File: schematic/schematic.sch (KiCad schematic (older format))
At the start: 19 parts, among them J1 Conn_01x04, J2 Conn_01x04, J3 Conn_01x04, J4 Conn_01x04, J5 Conn_01x04, SW1 SW_Push_Dual, U1 STM32F401VETx, Y1 Crystal_GND24

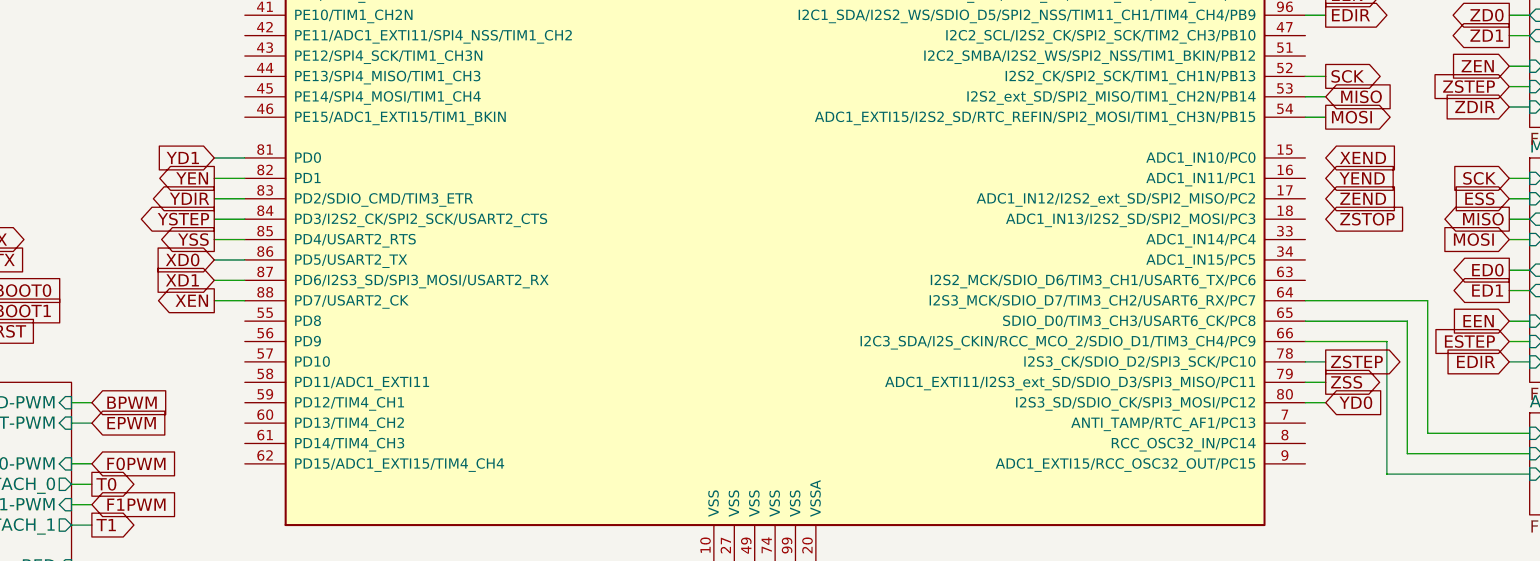
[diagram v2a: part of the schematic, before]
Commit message: Routed all control signals to drivers
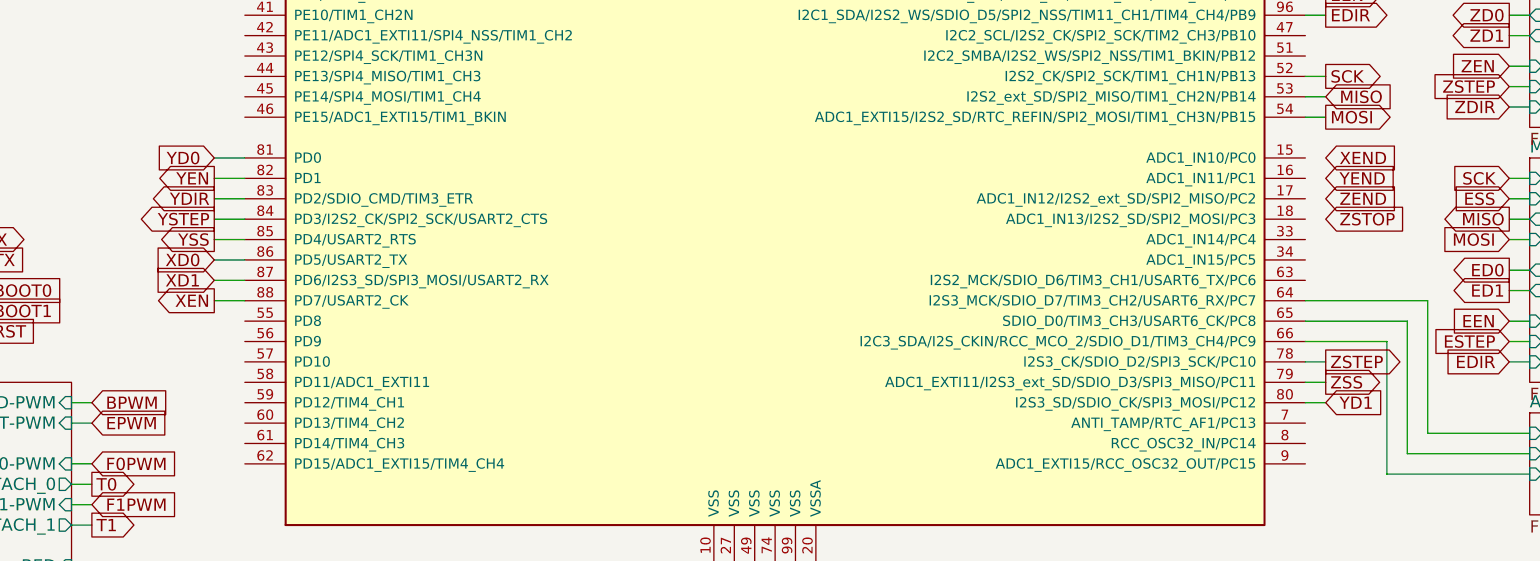
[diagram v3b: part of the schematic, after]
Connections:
- net YD0: now also U1.81 (PD0); no longer U1.80 (I2S3_SD/SDIO_CK/SPI3_MOSI/PC12)
- net YD1: now also U1.80 (I2S3_SD/SDIO_CK/SPI3_MOSI/PC12); no longer U1.81 (PD0)
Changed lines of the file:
@@
 	9100 1250 9200 1250
 Text GLabel 8200 5650 2    60   Input ~ 0
+YD1
+Text GLabel 2750 4450 0    60   Input ~ 0
 YD0
-Text GLabel 2750 4450 0    60   Input ~ 0
-YD1
 Text GLabel 2750 4550 0    60   Output ~ 0
 YEN

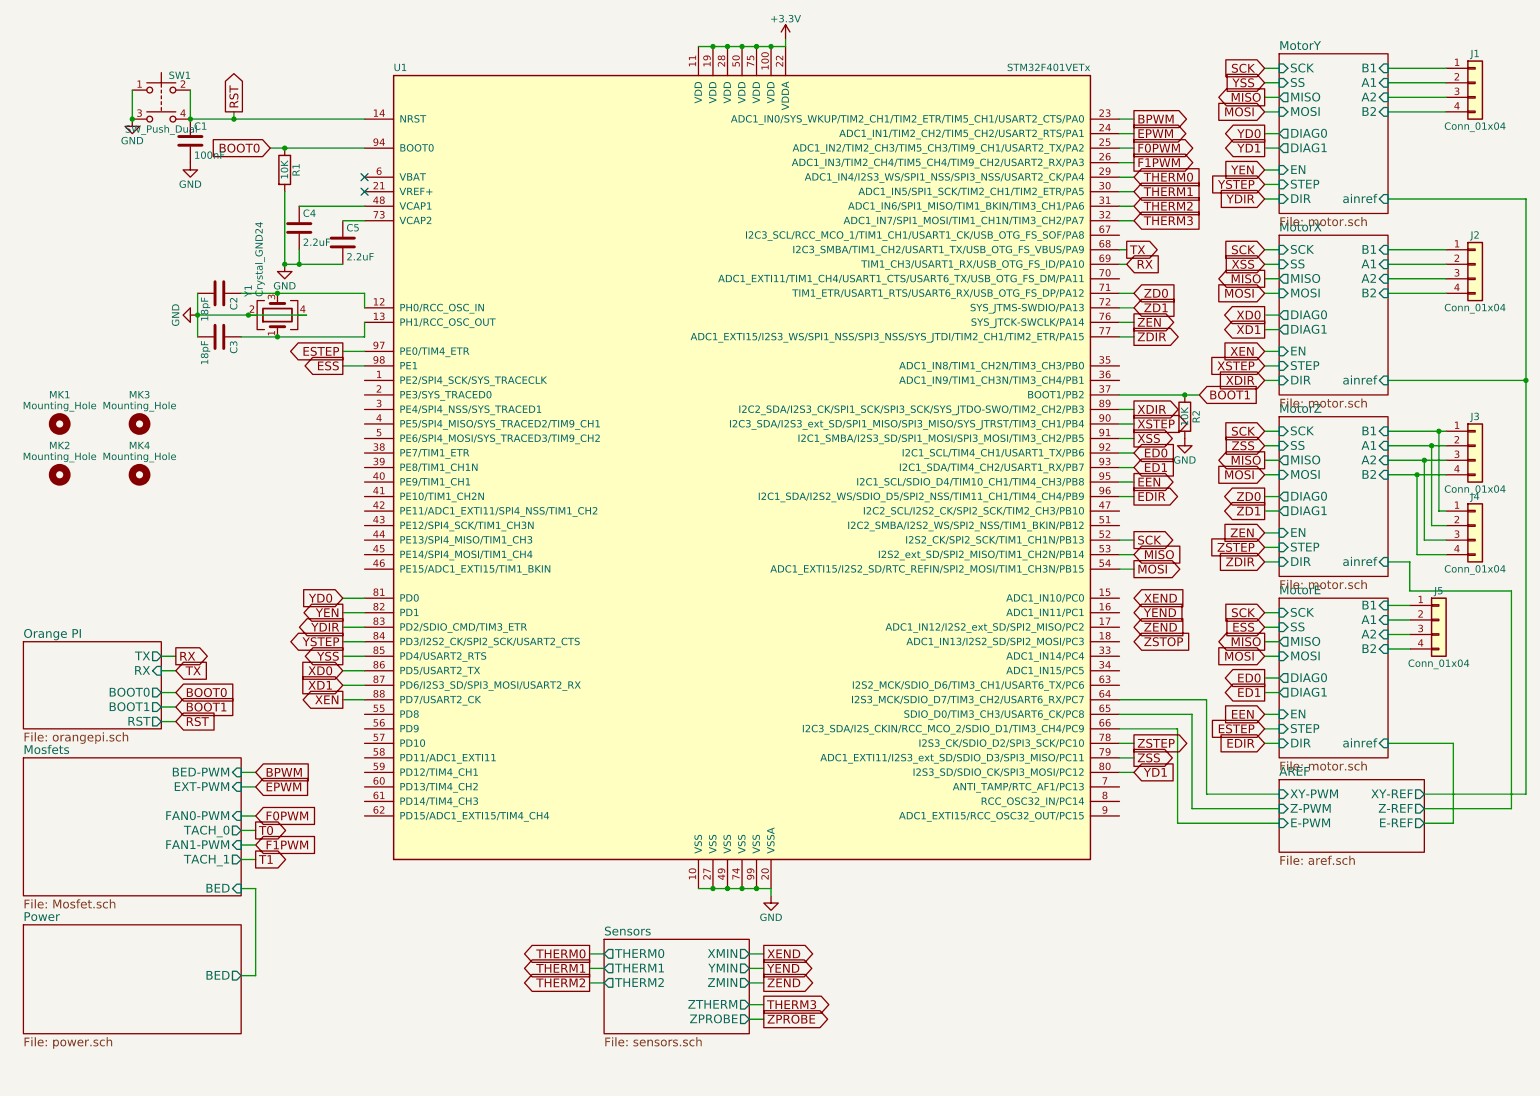
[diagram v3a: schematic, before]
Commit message: Added display headers
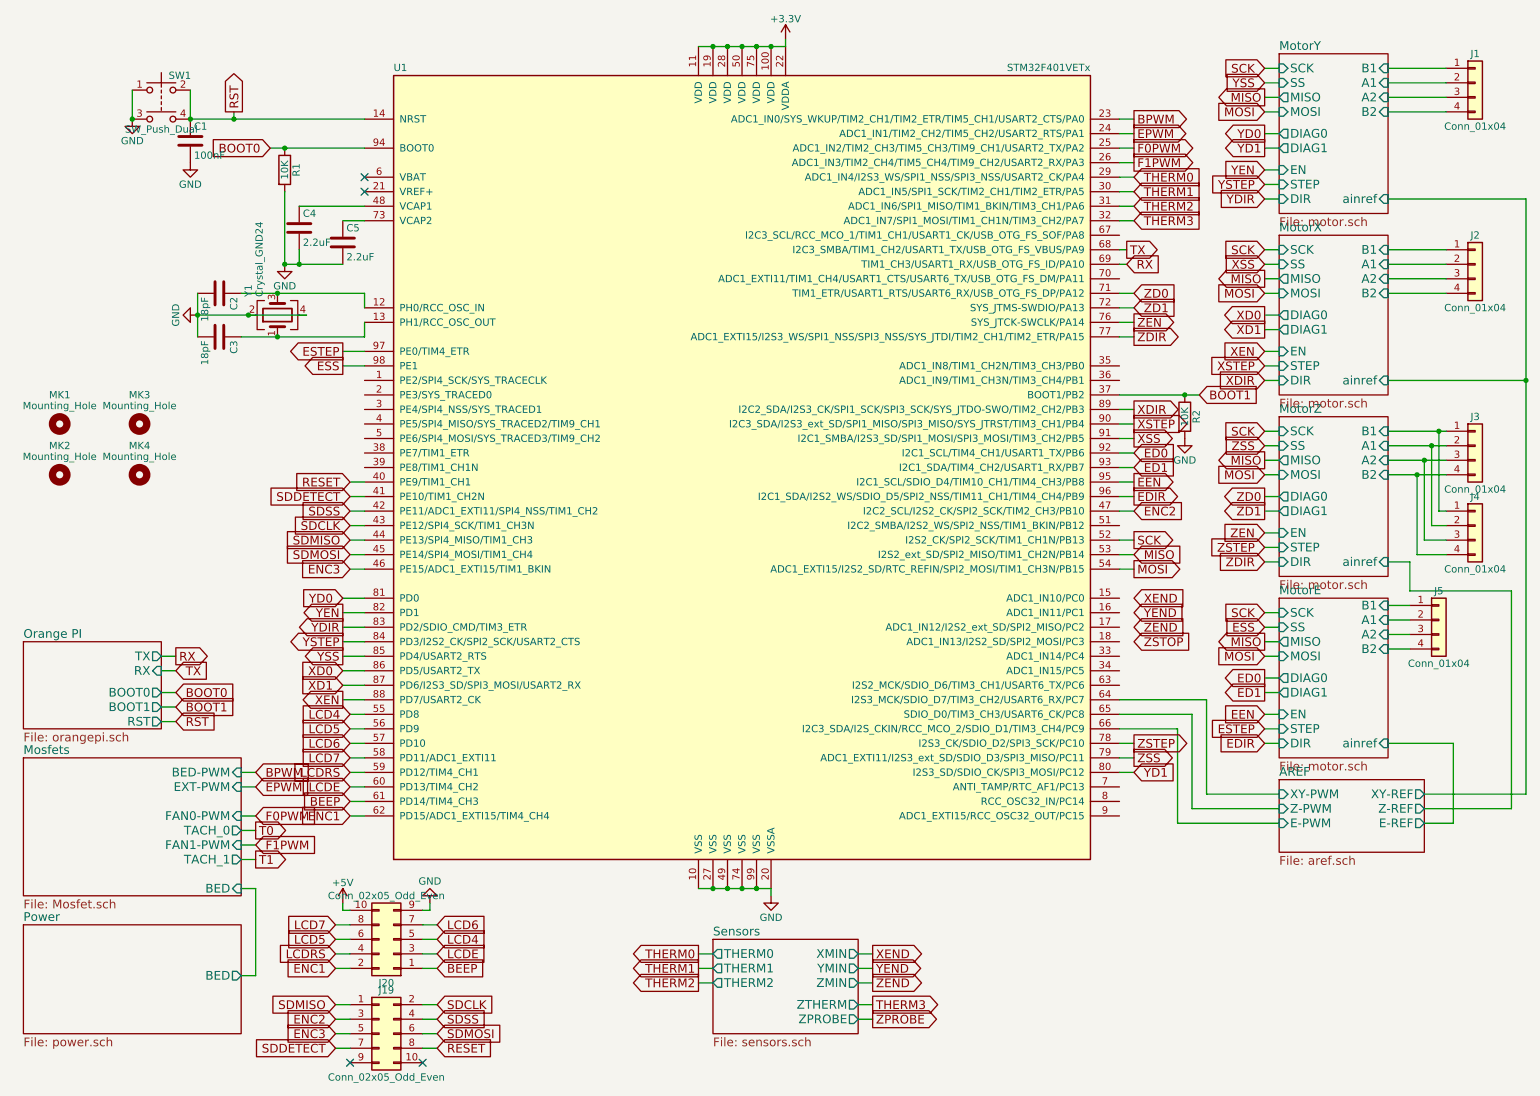
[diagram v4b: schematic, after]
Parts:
- added J19, J20: Conn_02x05_Odd_Even, Connectors:IDC_Header_Straight_10pins, symbol Conn_02x05_Odd_Even
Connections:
- net GND: now also J20.9 (Pin_9)
- net RESET: now reaches U1.40 (PE9/TIM1_CH1)
- net RESET: now also J19.8 (Pin_8)
- net SDDETECT: now reaches U1.41 (PE10/TIM1_CH2N)
- net SDDETECT: now also J19.7 (Pin_7)
- net SDSS: now reaches U1.42 (PE11/ADC1_EXTI11/SPI4_NSS/TIM1_CH2)
- net SDSS: now also J19.4 (Pin_4)
- net SDCLK: now reaches U1.43 (PE12/SPI4_SCK/TIM1_CH3N)
- net SDCLK: now also J19.2 (Pin_2)
- net SDMISO: now reaches U1.44 (PE13/SPI4_MISO/TIM1_CH3)
- net SDMISO: now also J19.1 (Pin_1)
- net SDMOSI: now reaches U1.45 (PE14/SPI4_MOSI/TIM1_CH4)
- net SDMOSI: now also J19.6 (Pin_6)
- net ENC3: now reaches U1.46 (PE15/ADC1_EXTI15/TIM1_BKIN)
- net ENC3: now also J19.5 (Pin_5)
- net ENC2: now reaches U1.47 (I2C2_SCL/I2S2_CK/SPI2_SCK/TIM2_CH3/PB10)
- net ENC2: now also J19.3 (Pin_3)
- net LCD4: now reaches U1.55 (PD8)
- net LCD4: now also J20.5 (Pin_5)
- net LCD5: now reaches U1.56 (PD9)
- net LCD5: now also J20.6 (Pin_6)
- net LCD6: now reaches U1.57 (PD10)
- net LCD6: now also J20.7 (Pin_7)
- net LCD7: now reaches U1.58 (PD11/ADC1_EXTI11)
- net LCD7: now also J20.8 (Pin_8)
- net LCDRS: now reaches U1.59 (PD12/TIM4_CH1)
- net LCDRS: now also J20.4 (Pin_4)
- net LCDE: now reaches U1.60 (PD13/TIM4_CH2)
- net LCDE: now also J20.3 (Pin_3)
- net BEEP: now reaches U1.61 (PD14/TIM4_CH3)
- net BEEP: now also J20.1 (Pin_1)
- net ENC1: now reaches U1.62 (PD15/ADC1_EXTI15/TIM4_CH4)
- net ENC1: now also J20.2 (Pin_2)
- new net +5V: J20.10 (Pin_10)
- no-connect marks 2 -> 4
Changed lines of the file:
@@
 $EndSheet
 $Sheet
-S 4550 6800 1000 650
+S 5300 6800 1000 650
 U 59ECE985
 F0 "Sensors" 60
 F1 "sensors.sch" 60
-F2 "THERM0" O L 4550 6900 60
-F3 "THERM1" O L 4550 7000 60
-F4 "THERM2" O L 4550 7100 60
-F5 "XMIN" O R 5550 6900 60
-F6 "YMIN" O R 5550 7000 60
-F7 "ZMIN" O R 5550 7100 60
-F8 "ZTHERM" O R 5550 7250 60
-F9 "ZPROBE" O R 5550 7350 60
+F2 "THERM0" O L 5300 6900 60
+F3 "THERM1" O L 5300 7000 60
+F4 "THERM2" O L 5300 7100 60
+F5 "XMIN" O R 6300 6900 60
+F6 "YMIN" O R 6300 7000 60
+F7 "ZMIN" O R 6300 7100 60
+F8 "ZTHERM" O R 6300 7250 60
+F9 "ZPROBE" O R 6300 7350 60
 $EndSheet
 $Sheet
@@
 Text GLabel 8200 1850 2    60   Input ~ 0
 THERM3
-Text GLabel 4450 6900 0    60   Output ~ 0
+Text GLabel 5200 6900 0    60   Output ~ 0
 THERM0
-Text GLabel 4450 7000 0    60   Output ~ 0
+Text GLabel 5200 7000 0    60   Output ~ 0
 THERM1
-Text GLabel 4450 7100 0    60   Output ~ 0
+Text GLabel 5200 7100 0    60   Output ~ 0
 THERM2
-Text GLabel 5650 7250 2    60   Output ~ 0
+Text GLabel 6400 7250 2    60   Output ~ 0
 THERM3
 Wire Wire Line
-	4450 6900 4550 6900
-Wire Wire Line
-	4450 7000 4550 7000
-Wire Wire Line
-	4450 7100 4550 7100
-Wire Wire Line
-	5650 7250 5550 7250
+	5200 6900 5300 6900
+Wire Wire Line
+	5200 7000 5300 7000
+Wire Wire Line
+	5200 7100 5300 7100
+Wire Wire Line
+	6400 7250 6300 7250
 Wire Wire Line
 	8100 1550 8200 1550
@@
 Text GLabel 8200 4750 2    60   Input ~ 0
 ZSTOP
-Text GLabel 5650 6900 2    60   Output ~ 0
+Text GLabel 6400 6900 2    60   Output ~ 0
 XEND
-Text GLabel 5650 7000 2    60   Output ~ 0
+Text GLabel 6400 7000 2    60   Output ~ 0
 YEND
-Text GLabel 5650 7100 2    60   Output ~ 0
+Text GLabel 6400 7100 2    60   Output ~ 0
 ZEND
-Text GLabel 5650 7350 2    60   Output ~ 0
+Text GLabel 6400 7350 2    60   Output ~ 0
 ZPROBE
 Wire Wire Line
-	5550 6900 5650 6900
-Wire Wire Line
-	5550 7000 5650 7000
-Wire Wire Line
-	5550 7100 5650 7100
-Wire Wire Line
-	5550 7350 5650 7350
+	6300 6900 6400 6900
+Wire Wire Line
+	6300 7000 6400 7000
+Wire Wire Line
+	6300 7100 6400 7100
+Wire Wire Line
+	6300 7350 6400 7350
 $Comp
 L Conn_01x04 J4
@@
 Wire Wire Line
 	8100 2450 8200 2450
+$Comp
+L Conn_02x05_Odd_Even J20
+U 1 1 5A71A41A
+P 3100 6800
+F 0 "J20" H 3150 7100 50  0000 C CNN
+F 1 "Conn_02x05_Odd_Even" H 3150 6500 50  0000 C CNN
+F 2 "Connectors:IDC_Header_Straight_10pins" H 3100 6800 50  0001 C CNN
+F 3 "" H 3100 6800 50  0001 C CNN
+	1    3100 6800
+	-1   0    0    1
+$EndComp
+$Comp
+L Conn_02x05_Odd_Even J19
+U 1 1 5A71A6D7
+P 3000 7450
+F 0 "J19" H 3050 7750 50  0000 C CNN
+F 1 "Conn_02x05_Odd_Even" H 3050 7150 50  0000 C CNN
+F 2 "Connectors:IDC_Header_Straight_10pins" H 3000 7450 50  0001 C CNN
+F 3 "" H 3000 7450 50  0001 C CNN
+	1    3000 7450
+	1    0    0    -1
+$EndComp
+$Comp
+L +5V #PWR08
+U 1 1 5A71CAE9
+P 2750 6550
+F 0 "#PWR08" H 2750 6400 50  0001 C CNN
+F 1 "+5V" H 2750 6690 50  0000 C CNN
+F 2 "" H 2750 6550 50  0001 C CNN
+F 3 "" H 2750 6550 50  0001 C CNN
+	1    2750 6550
+	1    0    0    -1
+$EndComp
+$Comp
+L GND #PWR09
+U 1 1 5A71CE27
+P 3350 6550
+F 0 "#PWR09" H 3350 6300 50  0001 C CNN
+F 1 "GND" H 3350 6400 50  0000 C CNN
+F 2 "" H 3350 6550 50  0001 C CNN
+F 3 "" H 3350 6550 50  0001 C CNN
+	1    3350 6550
+	-1   0    0    1
+$EndComp
+Wire Wire Line
+	3300 6600 3350 6600
+Wire Wire Line
+	3350 6600 3350 6550
+Wire Wire Line
+	2800 6600 2750 6600
+Wire Wire Line
+	2750 6600 2750 6550
+Text GLabel 2700 7250 0    60   Input ~ 0
+SDMISO
+Text GLabel 3400 7250 2    60   Input ~ 0
+SDCLK
+Text GLabel 3400 7350 2    60   Input ~ 0
+SDSS
+Text GLabel 3400 7450 2    60   Input ~ 0
+SDMOSI
+Text GLabel 3400 7550 2    60   Input ~ 0
+RESET
+Text GLabel 2700 7550 0    60   Input ~ 0
+SDDETECT
+Text GLabel 2700 6700 0    60   Input ~ 0
+LCD7
+Text GLabel 2700 6800 0    60   Input ~ 0
+LCD5
+Text GLabel 2700 6900 0    60   Input ~ 0
+LCDRS
+Text GLabel 3400 6700 2    60   Input ~ 0
+LCD6
+Text GLabel 3400 6800 2    60   Input ~ 0
+LCD4
+Text GLabel 3400 6900 2    60   Input ~ 0
+LCDE
+Text GLabel 3400 7000 2    60   Input ~ 0
+BEEP
+Text GLabel 2700 7000 0    60   Input ~ 0
+ENC1
+Text GLabel 2700 7350 0    60   Input ~ 0
+ENC2
+Text GLabel 2700 7450 0    60   Input ~ 0
+ENC3
+Wire Wire Line
+	2700 6700 2800 6700
+Wire Wire Line
+	2700 6800 2800 6800
+Wire Wire Line
+	2700 6900 2800 6900
+Wire Wire Line
+	2700 7000 2800 7000
+Wire Wire Line
+	3300 7000 3400 7000
+Wire Wire Line
+	3300 6900 3400 6900
+Wire Wire Line
+	3300 6800 3400 6800
+Wire Wire Line
+	3300 6700 3400 6700
+Wire Wire Line
+	2700 7250 2800 7250
+Wire Wire Line
+	2700 7350 2800 7350
+Wire Wire Line
+	2700 7450 2800 7450
+Wire Wire Line
+	2700 7550 2800 7550
+Wire Wire Line
+	3300 7250 3400 7250
+Wire Wire Line
+	3300 7350 3400 7350
+Wire Wire Line
+	3300 7450 3400 7450
+Wire Wire Line
+	3300 7550 3400 7550
+NoConn ~ 3300 7650
+NoConn ~ 2800 7650
+Text GLabel 2800 3950 0    60   Input ~ 0
+SDCLK
+Text GLabel 2800 4050 0    60   Input ~ 0
+SDMISO
+Text GLabel 2800 4150 0    60   Input ~ 0
+SDMOSI
+Wire Wire Line
+	2900 3950 2800 3950
+Wire Wire Line
+	2800 4050 2900 4050
+Wire Wire Line
+	2900 4150 2800 4150
+Text GLabel 2800 3850 0    60   Input ~ 0
+SDSS
+Wire Wire Line
+	2800 3850 2900 3850
+Text GLabel 2800 3750 0    60   Input ~ 0
+SDDETECT
+Text GLabel 2800 3650 0    60   Input ~ 0
+RESET
+Text GLabel 8200 3850 2    60   Input ~ 0
+ENC2
+Text GLabel 2800 4250 0    60   Input ~ 0
+ENC3
+Wire Wire Line
+	8100 3850 8200 3850
+Wire Wire Line
+	2800 4250 2900 4250
+Wire Wire Line
+	2800 3650 2900 3650
+Wire Wire Line
+	2800 3750 2900 3750
+Text GLabel 2800 5250 0    60   Input ~ 0
+LCD4
+Text GLabel 2800 5350 0    60   Input ~ 0
+LCD5
+Text GLabel 2800 5450 0    60   Input ~ 0
+LCD6
+Text GLabel 2800 5550 0    60   Input ~ 0
+LCD7
+Text GLabel 2800 5650 0    60   Input ~ 0
+LCDRS
+Text GLabel 2800 5750 0    60   Input ~ 0
+LCDE
+Text GLabel 2800 5950 0    60   Input ~ 0
+ENC1
+Text GLabel 2800 5850 0    60   Input ~ 0
+BEEP
+Wire Wire Line
+	2800 5250 2900 5250
+Wire Wire Line
+	2800 5350 2900 5350
+Wire Wire Line
+	2800 5450 2900 5450
+Wire Wire Line
+	2800 5550 2900 5550
+Wire Wire Line
+	2800 5650 2900 5650
+Wire Wire Line
+	2800 5750 2900 5750
+Wire Wire Line
+	2800 5850 2900 5850
+Wire Wire Line
+	2800 5950 2900 5950
 $EndSCHEMATC

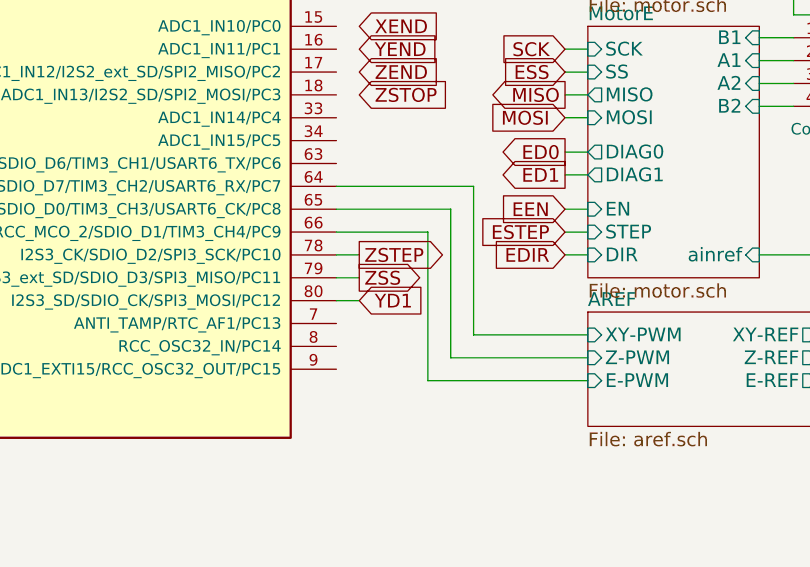
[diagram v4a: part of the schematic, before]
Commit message: Routed current pwm drivers
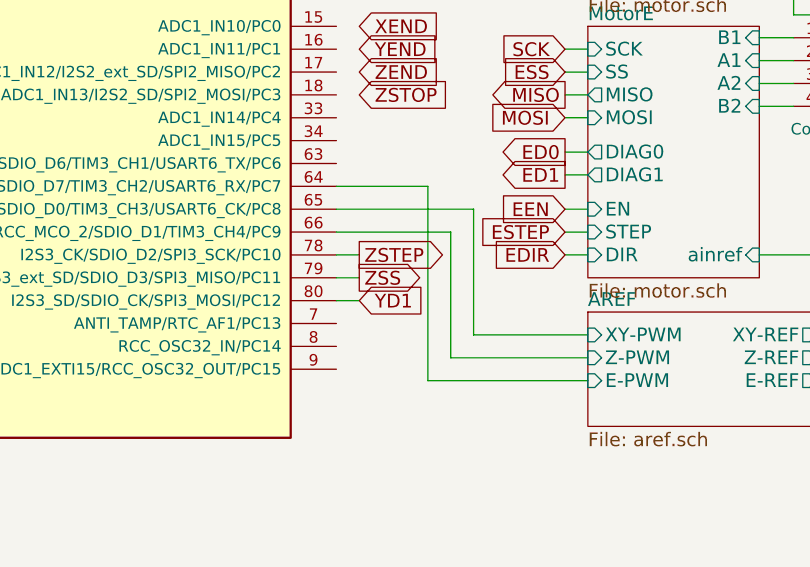
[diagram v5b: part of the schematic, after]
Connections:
- net AREF/E-PWM: now also U1.64 (I2S3_MCK/SDIO_D7/TIM3_CH2/USART6_RX/PC7); no longer U1.66 (I2C3_SDA/I2S_CKIN/RCC_MCO_2/SDIO_D1/TIM3_CH4/PC9)
- net AREF/XY-PWM: now also U1.65 (SDIO_D0/TIM3_CH3/USART6_CK/PC8); no longer U1.64 (I2S3_MCK/SDIO_D7/TIM3_CH2/USART6_RX/PC7)
- net AREF/Z-PWM: now also U1.66 (I2C3_SDA/I2S_CKIN/RCC_MCO_2/SDIO_D1/TIM3_CH4/PC9); no longer U1.65 (SDIO_D0/TIM3_CH3/USART6_CK/PC8)
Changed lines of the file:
@@
 ESS
 Wire Wire Line
-	8100 5150 8700 5150
-Wire Wire Line
-	8700 5150 8700 5800
-Wire Wire Line
 	8700 5800 9200 5800
 Wire Wire Line
-	8100 5250 8600 5250
-Wire Wire Line
-	8600 5250 8600 5900
+	8600 5350 8600 5900
 Wire Wire Line
 	8600 5900 9200 5900
 Wire Wire Line
-	8100 5350 8500 5350
-Wire Wire Line
-	8500 5350 8500 6000
+	8500 5150 8500 6000
 Wire Wire Line
 	8500 6000 9200 6000
@@
 Wire Wire Line
 	2800 5950 2900 5950
+Wire Wire Line
+	8100 5150 8500 5150
+Wire Wire Line
+	8600 5350 8100 5350
+Wire Wire Line
+	8100 5250 8700 5250
+Wire Wire Line
+	8700 5250 8700 5800
 $EndSCHEMATC
